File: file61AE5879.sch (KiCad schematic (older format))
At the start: 6 parts

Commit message: Merged 8254
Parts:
- gave numbers to parts that had none: 6
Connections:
- net CLK: now reaches U2.19 (CLK)
- net Reset: now reaches U2.21 (RESET)
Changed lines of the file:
@@
 $Descr A4 11693 8268
 encoding utf-8
-Sheet 3 6
+Sheet 2 8
 Title ""
 Date ""
@@
 $EndDescr
 $Comp
-L power:+5V #PWR?
+L power:+5V #PWR0103
 U 1 1 61B24927
 P 2250 900
-F 0 "#PWR?" H 2250 750 50  0001 C CNN
+F 0 "#PWR0103" H 2250 750 50  0001 C CNN
 F 1 "+5V" H 2265 1073 50  0000 C CNN
 F 2 "" H 2250 900 50  0001 C CNN
@@
 $EndComp
 $Comp
-L power:GND #PWR?
+L power:GND #PWR0104
 U 1 1 61B27567
 P 2150 4750
-F 0 "#PWR?" H 2150 4500 50  0001 C CNN
+F 0 "#PWR0104" H 2150 4500 50  0001 C CNN
 F 1 "GND" H 2155 4577 50  0000 C CNN
 F 2 "" H 2150 4750 50  0001 C CNN
@@
 $EndComp
 $Comp
-L 74xx:74LS245 U?
+L 74xx:74LS245 U4
 U 1 1 61B337B6
 P 4450 4050
-F 0 "U?" H 4450 5031 50  0000 C CNN
+F 0 "U4" H 4450 5031 50  0000 C CNN
 F 1 "74LS245" H 4450 4940 50  0000 C CNN
 F 2 "" H 4450 4050 50  0001 C CNN
@@
 	2250 900  2250 1150
 $Comp
-L power:GND #PWR?
+L power:GND #PWR0105
 U 1 1 61B25E9F
 P 2350 4750
-F 0 "#PWR?" H 2350 4500 50  0001 C CNN
+F 0 "#PWR0105" H 2350 4500 50  0001 C CNN
 F 1 "GND" H 2355 4577 50  0000 C CNN
 F 2 "" H 2350 4750 50  0001 C CNN
@@
 	2900 1650 2950 1650
 $Comp
-L 74xx:74LS245 U?
+L 74xx:74LS245 U3
 U 1 1 61B2B683
 P 4450 1900
-F 0 "U?" H 4450 2881 50  0000 C CNN
+F 0 "U3" H 4450 2881 50  0000 C CNN
 F 1 "74LS245" H 4450 2790 50  0000 C CNN
 F 2 "" H 4450 1900 50  0001 C CNN
@@
 $EndComp
 $Comp
-L power:GND #PWR?
+L power:GND #PWR0106
 U 1 1 61B66AC8
 P 4450 4850
-F 0 "#PWR?" H 4450 4600 50  0001 C CNN
+F 0 "#PWR0106" H 4450 4600 50  0001 C CNN
 F 1 "GND" H 4455 4677 50  0000 C CNN
 F 2 "" H 4450 4850 50  0001 C CNN
@@
 $EndComp
 $Comp
-L power:+5V #PWR?
+L power:+5V #PWR0107
 U 1 1 61B68EE0
 P 1550 4450
-F 0 "#PWR?" H 1550 4300 50  0001 C CNN
+F 0 "#PWR0107" H 1550 4300 50  0001 C CNN
 F 1 "+5V" V 1565 4578 50  0000 L CNN
 F 2 "" H 1550 4450 50  0001 C CNN
@@
 $EndComp
 $Comp
-L 74xx:74LS373 U?
+L 74xx:74LS373 U7
 U 1 1 61B8BD15
 P 5950 6100
-F 0 "U?" H 5950 7081 50  0000 C CNN
+F 0 "U7" H 5950 7081 50  0000 C CNN
 F 1 "74LS373" H 5950 6990 50  0000 C CNN
 F 2 "" H 5950 6100 50  0001 C CNN
@@
 NoConn ~ 6450 6300
 $Comp
-L power:+5V #PWR?
+L power:+5V #PWR0108
 U 1 1 61BADFEF
 P 4450 3250
-F 0 "#PWR?" H 4450 3100 50  0001 C CNN
+F 0 "#PWR0108" H 4450 3100 50  0001 C CNN
 F 1 "+5V" V 4465 3378 50  0000 L CNN
 F 2 "" H 4450 3250 50  0001 C CNN
@@
 $EndComp
 $Comp
-L power:+5V #PWR?
+L power:+5V #PWR0109
 U 1 1 61BB157C
 P 4450 1100
-F 0 "#PWR?" H 4450 950 50  0001 C CNN
+F 0 "#PWR0109" H 4450 950 50  0001 C CNN
 F 1 "+5V" V 4465 1228 50  0000 L CNN
 F 2 "" H 4450 1100 50  0001 C CNN
@@
 $EndComp
 $Comp
-L power:+5V #PWR?
+L power:+5V #PWR0110
 U 1 1 61BB1E99
 P 5950 5300
-F 0 "#PWR?" H 5950 5150 50  0001 C CNN
+F 0 "#PWR0110" H 5950 5150 50  0001 C CNN
 F 1 "+5V" V 5965 5428 50  0000 L CNN
 F 2 "" H 5950 5300 50  0001 C CNN
@@
 $EndComp
 $Comp
-L power:GND #PWR?
+L power:GND #PWR0111
 U 1 1 61BB3E62
 P 5450 6600
-F 0 "#PWR?" H 5450 6350 50  0001 C CNN
+F 0 "#PWR0111" H 5450 6350 50  0001 C CNN
 F 1 "GND" H 5455 6427 50  0000 C CNN
 F 2 "" H 5450 6600 50  0001 C CNN
@@
 $EndComp
 $Comp
-L power:GND #PWR?
+L power:GND #PWR0112
 U 1 1 61BB4868
 P 5950 6900
-F 0 "#PWR?" H 5950 6650 50  0001 C CNN
+F 0 "#PWR0112" H 5950 6650 50  0001 C CNN
 F 1 "GND" H 5955 6727 50  0000 C CNN
 F 2 "" H 5950 6900 50  0001 C CNN
@@
 	2900 1450 2950 1450
 $Comp
-L MCU_Intel:8086_Min_Mode U?
+L MCU_Intel:8086_Min_Mode U2
 U 1 1 61AE6FB5
 P 2250 2950
-F 0 "U?" H 2250 4931 50  0000 C CNN
+F 0 "U2" H 2250 4931 50  0000 C CNN
 F 1 "8086_Min_Mode" H 2250 4840 50  0000 C CNN
 F 2 "Package_DIP:DIP-40_W15.24mm" H 2300 3050 50  0001 C CIN
@@
 	5400 3550 5450 3550
 $Comp
-L power:+5V #PWR?
+L power:+5V #PWR0113
 U 1 1 61BAEB1C
 P 5950 3250
-F 0 "#PWR?" H 5950 3100 50  0001 C CNN
+F 0 "#PWR0113" H 5950 3100 50  0001 C CNN
 F 1 "+5V" V 5965 3378 50  0000 L CNN
 F 2 "" H 5950 3250 50  0001 C CNN
@@
 	5450 4450 5200 4450
 $Comp
+L power:GND #PWR0115
+U 1 1 61BB3576
+P 5450 4550
+F 0 "#PWR0115" H 5450 4300 50  0001 C CNN
+F 1 "GND" H 5455 4377 50  0000 C CNN
+F 2 "" H 5450 4550 50  0001 C CNN
+F 3 "" H 5450 4550 50  0001 C CNN
+	1    5450 4550
+	1    0    0    -1
+$EndComp
+$Comp
+L 74xx:74LS373 U6
+U 1 1 61B45F86
+P 5950 4050
+F 0 "U6" H 5950 5031 50  0000 C CNN
+F 1 "74LS373" H 5950 4940 50  0000 C CNN
+F 2 "" H 5950 4050 50  0001 C CNN
+F 3 "http://www.ti.com/lit/gpn/sn74LS373" H 5950 4050 50  0001 C CNN
+	1    5950 4050
+	1    0    0    -1
+$EndComp
+Wire Wire Line
+	6450 1700 6550 1700
+Wire Wire Line
+	5400 1700 5450 1700
+Wire Wire Line
+	5400 1600 5450 1600
+Wire Wire Line
+	6450 1600 6550 1600
+Wire Wire Line
+	6450 1500 6550 1500
+Wire Wire Line
+	5400 1500 5450 1500
+Wire Wire Line
+	5400 1400 5450 1400
+$Comp
+L power:+5V #PWR0116
+U 1 1 61BAFB11
+P 5950 1100
+F 0 "#PWR0116" H 5950 950 50  0001 C CNN
+F 1 "+5V" V 5965 1228 50  0000 L CNN
+F 2 "" H 5950 1100 50  0001 C CNN
+F 3 "" H 5950 1100 50  0001 C CNN
+	1    5950 1100
+	0    1    1    0
+$EndComp
+Wire Wire Line
+	6450 1400 6550 1400
+Wire Wire Line
+	6450 2100 6550 2100
+Wire Wire Line
+	5400 2100 5450 2100
+Wire Wire Line
+	5400 2000 5450 2000
+Wire Wire Line
+	6450 2000 6550 2000
+Wire Wire Line
+	6450 1900 6550 1900
+Wire Wire Line
+	5400 1900 5450 1900
+Wire Wire Line
+	5400 1800 5450 1800
+Wire Wire Line
+	6450 1800 6550 1800
+Wire Wire Line
+	5350 2300 5450 2300
+$Comp
+L power:GND #PWR0117
+U 1 1 61B651B8
+P 5950 2700
+F 0 "#PWR0117" H 5950 2450 50  0001 C CNN
+F 1 "GND" H 5955 2527 50  0000 C CNN
+F 2 "" H 5950 2700 50  0001 C CNN
+F 3 "" H 5950 2700 50  0001 C CNN
+	1    5950 2700
+	1    0    0    -1
+$EndComp
+$Comp
+L power:GND #PWR0118
+U 1 1 61B642BA
+P 5450 2400
+F 0 "#PWR0118" H 5450 2150 50  0001 C CNN
+F 1 "GND" H 5455 2227 50  0000 C CNN
+F 2 "" H 5450 2400 50  0001 C CNN
+F 3 "" H 5450 2400 50  0001 C CNN
+	1    5450 2400
+	1    0    0    -1
+$EndComp
+$Comp
+L 74xx:74LS373 U5
+U 1 1 61B4F7E5
+P 5950 1900
+F 0 "U5" H 5950 2881 50  0000 C CNN
+F 1 "74LS373" H 5950 2790 50  0000 C CNN
+F 2 "" H 5950 1900 50  0001 C CNN
+F 3 "http://www.ti.com/lit/gpn/sn74LS373" H 5950 1900 50  0001 C CNN
+	1    5950 1900
+	1    0    0    -1
+$EndComp
+Text HLabel 1550 1850 0    50   Input ~ 0
+Reset
+Text HLabel 1550 1450 0    50   Output ~ 0
+CLK
+Wire Bus Line
+	3800 1300 3800 2000
+Wire Bus Line
+	3800 3550 3800 4150
+Wire Bus Line
+	5300 1300 5300 2000
+Wire Bus Line
+	3100 2950 3100 3550
+Wire Bus Line
+	5300 2950 5300 4150
+Wire Bus Line
+	3100 2000 3100 2750
+Wire Bus Line
+	6650 1300 6650 6000
+Wire Bus Line
+	5100 1300 5100 4350
+$Comp
 L power:GND #PWR?
-U 1 1 61B65D27
+U 1 1 626757DE
 P 5950 4850
 F 0 "#PWR?" H 5950 4600 50  0001 C CNN
@@
 	1    0    0    -1
 $EndComp
-$Comp
-L power:GND #PWR?
-U 1 1 61BB3576
-P 5450 4550
-F 0 "#PWR?" H 5450 4300 50  0001 C CNN
-F 1 "GND" H 5455 4377 50  0000 C CNN
-F 2 "" H 5450 4550 50  0001 C CNN
-F 3 "" H 5450 4550 50  0001 C CNN
-	1    5450 4550
-	1    0    0    -1
-$EndComp
-$Comp
-L 74xx:74LS373 U?
-U 1 1 61B45F86
-P 5950 4050
-F 0 "U?" H 5950 5031 50  0000 C CNN
-F 1 "74LS373" H 5950 4940 50  0000 C CNN
-F 2 "" H 5950 4050 50  0001 C CNN
-F 3 "http://www.ti.com/lit/gpn/sn74LS373" H 5950 4050 50  0001 C CNN
-	1    5950 4050
-	1    0    0    -1
-$EndComp
-Wire Wire Line
-	6450 1700 6550 1700
-Wire Wire Line
-	5400 1700 5450 1700
-Wire Wire Line
-	5400 1600 5450 1600
-Wire Wire Line
-	6450 1600 6550 1600
-Wire Wire Line
-	6450 1500 6550 1500
-Wire Wire Line
-	5400 1500 5450 1500
-Wire Wire Line
-	5400 1400 5450 1400
-$Comp
-L power:+5V #PWR?
-U 1 1 61BAFB11
-P 5950 1100
-F 0 "#PWR?" H 5950 950 50  0001 C CNN
-F 1 "+5V" V 5965 1228 50  0000 L CNN
-F 2 "" H 5950 1100 50  0001 C CNN
-F 3 "" H 5950 1100 50  0001 C CNN
-	1    5950 1100
-	0    1    1    0
-$EndComp
-Wire Wire Line
-	6450 1400 6550 1400
-Wire Wire Line
-	6450 2100 6550 2100
-Wire Wire Line
-	5400 2100 5450 2100
-Wire Wire Line
-	5400 2000 5450 2000
-Wire Wire Line
-	6450 2000 6550 2000
-Wire Wire Line
-	6450 1900 6550 1900
-Wire Wire Line
-	5400 1900 5450 1900
-Wire Wire Line
-	5400 1800 5450 1800
-Wire Wire Line
-	6450 1800 6550 1800
-Wire Wire Line
-	5350 2300 5450 2300
-$Comp
-L power:GND #PWR?
-U 1 1 61B651B8
-P 5950 2700
-F 0 "#PWR?" H 5950 2450 50  0001 C CNN
-F 1 "GND" H 5955 2527 50  0000 C CNN
-F 2 "" H 5950 2700 50  0001 C CNN
-F 3 "" H 5950 2700 50  0001 C CNN
-	1    5950 2700
-	1    0    0    -1
-$EndComp
-$Comp
-L power:GND #PWR?
-U 1 1 61B642BA
-P 5450 2400
-F 0 "#PWR?" H 5450 2150 50  0001 C CNN
-F 1 "GND" H 5455 2227 50  0000 C CNN
-F 2 "" H 5450 2400 50  0001 C CNN
-F 3 "" H 5450 2400 50  0001 C CNN
-	1    5450 2400
-	1    0    0    -1
-$EndComp
-$Comp
-L 74xx:74LS373 U?
-U 1 1 61B4F7E5
-P 5950 1900
-F 0 "U?" H 5950 2881 50  0000 C CNN
-F 1 "74LS373" H 5950 2790 50  0000 C CNN
-F 2 "" H 5950 1900 50  0001 C CNN
-F 3 "http://www.ti.com/lit/gpn/sn74LS373" H 5950 1900 50  0001 C CNN
-	1    5950 1900
-	1    0    0    -1
-$EndComp
-Wire Bus Line
-	3800 1300 3800 2000
-Wire Bus Line
-	3800 3550 3800 4150
-Wire Bus Line
-	5300 1300 5300 2000
-Wire Bus Line
-	3100 2950 3100 3550
-Wire Bus Line
-	5300 2950 5300 4150
-Wire Bus Line
-	3100 2000 3100 2750
-Wire Bus Line
-	6650 1300 6650 6000
-Wire Bus Line
-	5100 1300 5100 4350
 $EndSCHEMATC

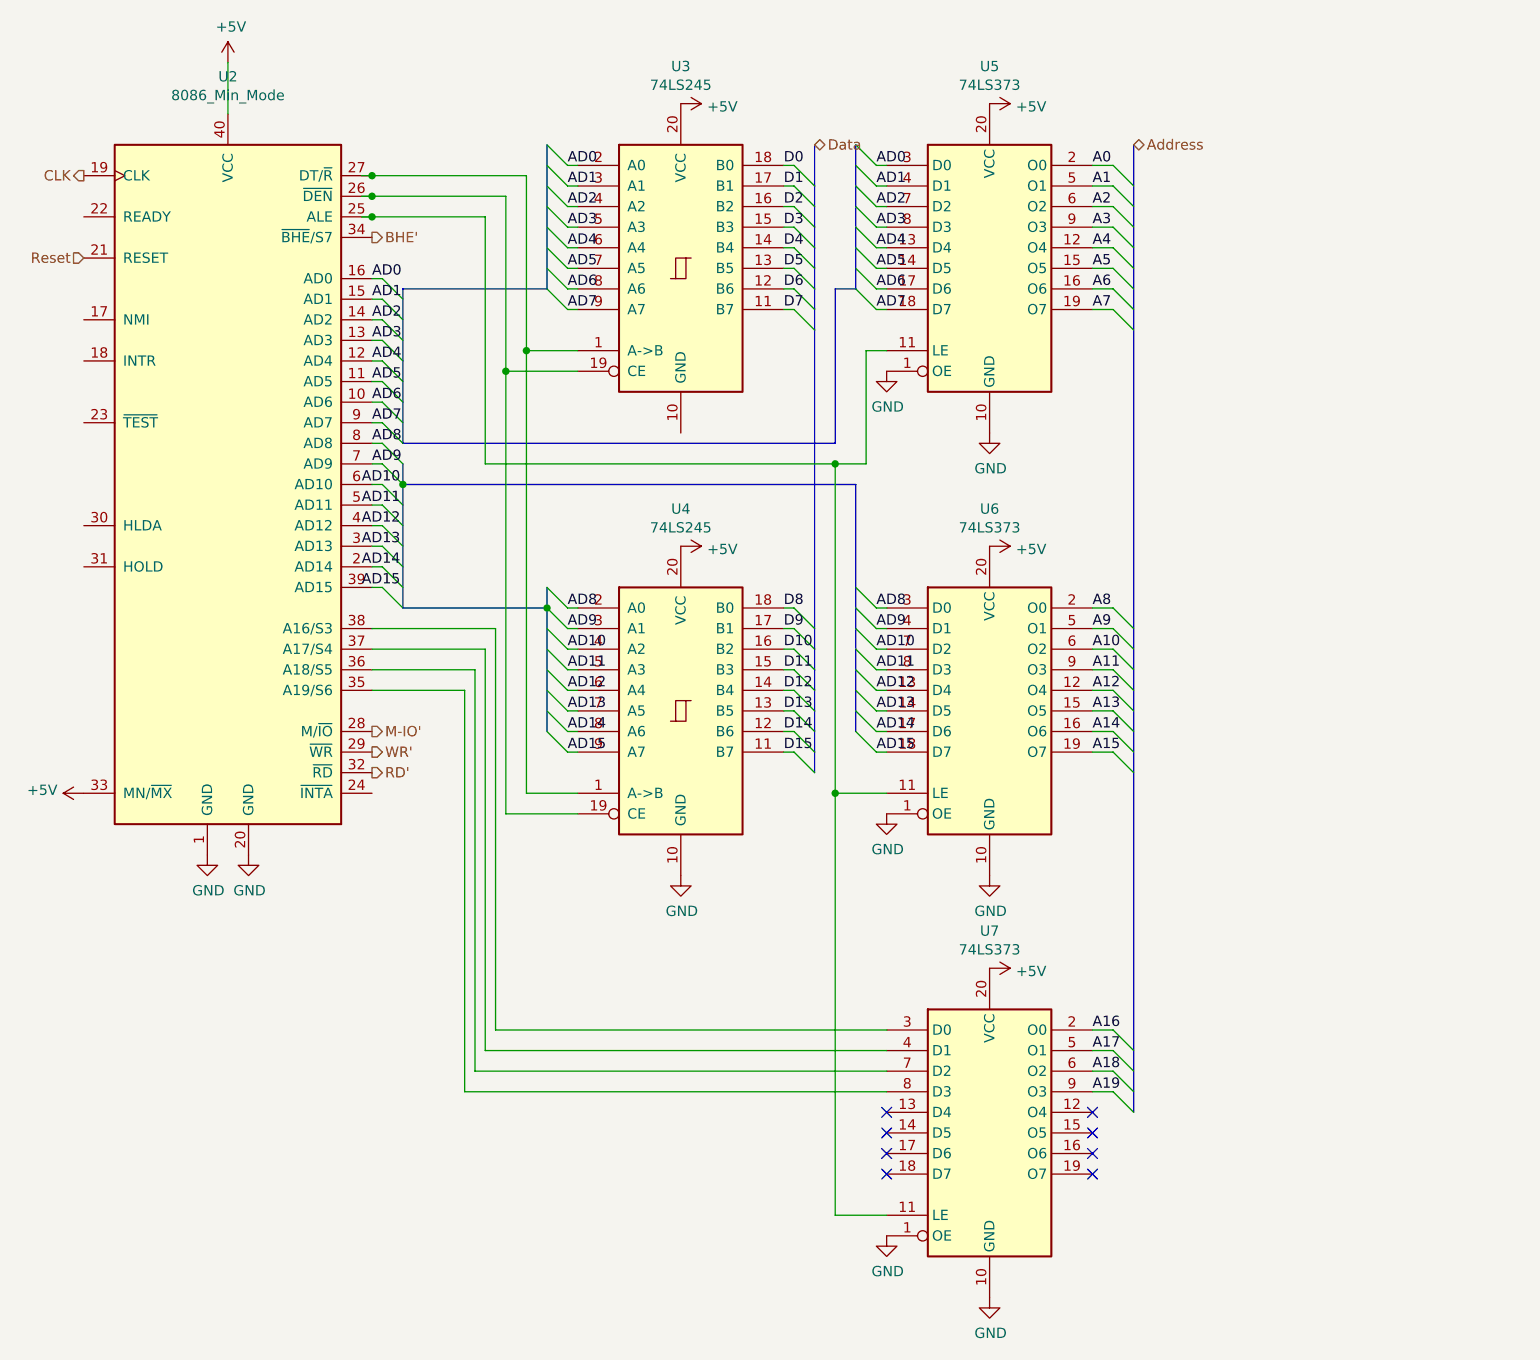
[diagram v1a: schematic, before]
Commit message: Integrated LCD.  Fixed issues with busses
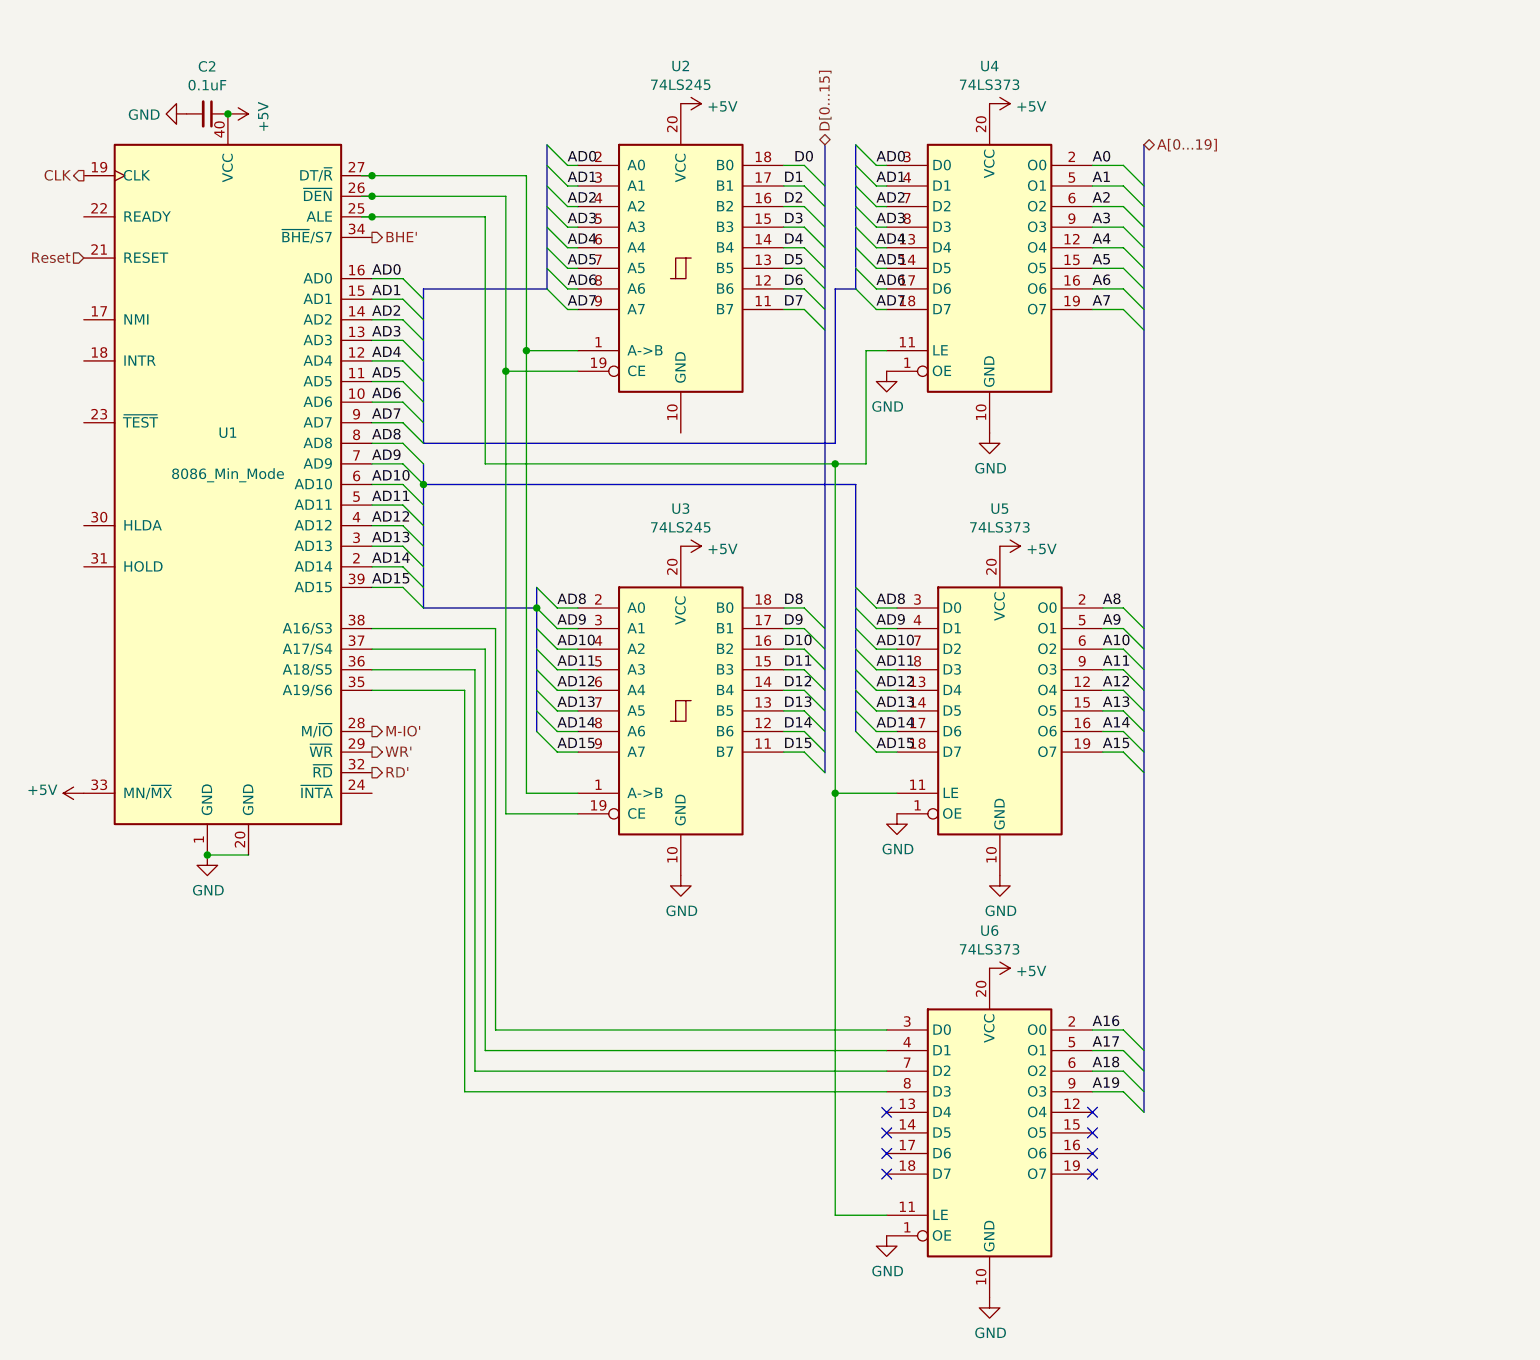
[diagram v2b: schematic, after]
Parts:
- added C2: 0.1uF, symbol Device:C_Small
- renumbered U2 to U1, U3 to U2, U4 to U3, U5 to U4, U6 to U5, U7 to U6
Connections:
- net +5V: now also C2.1
- net AD10: now also U1.6 (AD10)
- net AD11: now also U1.5 (AD11)
- net AD12: now also U1.4 (AD12)
- net AD13: now also U1.3 (AD13)
- net AD14: now also U1.2 (AD14)
- net AD15: now also U1.39 (AD15)
- net GND: now also C2.2
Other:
- moved on the sheet: U5

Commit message: Wired Root
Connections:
- net NMI: now reaches U1.17 (NMI)
- net INTR: now reaches U1.18 (INTR)
- net Ready: now reaches U1.22 (READY)
- net INTA': now reaches U1.24 (~INTA~)
- no-connect marks 8 -> 11
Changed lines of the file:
@@
 $Descr A4 11693 8268
 encoding utf-8
-Sheet 2 12
+Sheet 2 13
 Title ""
 Date ""
@@
 Wire Wire Line
 	2350 4750 2150 4750
+Connection ~ 2150 4750
+Text HLabel 2950 4450 2    50   Input ~ 0
+INTA'
+NoConn ~ 1550 3150
+NoConn ~ 1550 3350
+NoConn ~ 1550 2650
 Wire Bus Line
 	3800 1300 3800 2000
@@
 Wire Bus Line
 	6700 1300 6700 6000
-Connection ~ 2150 4750
+Text HLabel 1550 1650 0    50   Input ~ 0
+Ready
+Text HLabel 1550 2150 0    50   Input ~ 0
+NMI
+Text HLabel 1550 2350 0    50   Input ~ 0
+INTR
 $EndSCHEMATC

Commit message: Started PCB
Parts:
- added J2: Conn_01x20, Connector:Banana_Jack_1Pin, symbol Connector_Generic:Conn_01x20
- added J3: Conn_01x16, Connector:Banana_Jack_1Pin, symbol Connector_Generic:Conn_01x16
- added J4: Conn_01x10, Connector:Banana_Jack_1Pin, symbol Connector_Generic:Conn_01x10
- C2: footprint (none) -> Capacitor_SMD:CP_Elec_3x5.3
- U2, U3, U4: footprint (none) -> Package_DIP:DIP-20_W7.62mm
- U5: renamed from U6; footprint (none) -> Package_DIP:DIP-20_W7.62mm
- U6: renamed from U5; footprint (none) -> Package_DIP:DIP-20_W7.62mm
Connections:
- net A0: now also J2.1 (Pin_1)
- net A1: now also J2.2 (Pin_2)
- net A10: now also J2.11 (Pin_11)
- net A11: now also J2.12 (Pin_12)
- net A12: now also J2.13 (Pin_13)
- net A13: now also J2.14 (Pin_14)
- net A14: now also J2.15 (Pin_15)
- net A15: now also J2.16 (Pin_16)
- net A16: now also J2.17 (Pin_17)
- net A17: now also J2.18 (Pin_18)
- net A18: now also J2.19 (Pin_19)
- net A19: now also J2.20 (Pin_20)
- net A2: now also J2.3 (Pin_3)
- net A3: now also J2.4 (Pin_4)
- net A4: now also J2.5 (Pin_5)
- net A5: now also J2.6 (Pin_6)
- net A6: now also J2.7 (Pin_7)
- net A7: now also J2.8 (Pin_8)
- net A8: now also J2.9 (Pin_9)
- net A9: now also J2.10 (Pin_10)
- net BHE': now also J4.1 (Pin_1)
- net CLK: now also J4.6 (Pin_6)
- net D0: now also J3.1 (Pin_1)
- net D1: now also J3.2 (Pin_2)
- net D10: now also J3.11 (Pin_11)
- net D11: now also J3.12 (Pin_12)
- net D12: now also J3.13 (Pin_13)
- net D13: now also J3.14 (Pin_14)
- net D14: now also J3.15 (Pin_15)
- net D15: now also J3.16 (Pin_16)
- net D2: now also J3.3 (Pin_3)
- net D3: now also J3.4 (Pin_4)
- net D4: now also J3.5 (Pin_5)
- net D5: now also J3.6 (Pin_6)
- net D6: now also J3.7 (Pin_7)
- net D7: now also J3.8 (Pin_8)
- net D8: now also J3.9 (Pin_9)
- net D9: now also J3.10 (Pin_10)
- net GND: now also U2.10 (GND)
- net INTA': now also J4.2 (Pin_2)
- net INTR: now also J4.9 (Pin_9)
- net M-IO': now also J4.5 (Pin_5)
- net NMI: now also J4.7 (Pin_7)
- net RD': now also J4.3 (Pin_3)
- net Ready: now also J4.8 (Pin_8)
- net Reset: now also J4.10 (Pin_10)
- net WR': now also J4.4 (Pin_4)
